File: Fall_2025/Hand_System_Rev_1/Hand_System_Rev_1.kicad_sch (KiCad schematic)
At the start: 0 parts

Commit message: Changes
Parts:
- added C1: 22u, Capacitor_THT:CP_Radial_D4.0mm_P1.50mm, symbol Device:C
- added C2: 100 μF, symbol Device:C
- added H1, H2, H3, H4: MountingHole, symbol Mechanical:MountingHole
- added J1: Barrel_Jack, Connector_BarrelJack:BarrelJack_SwitchcraftConxall_RAPC10U_Horizontal, symbol Connector:Barrel_Jack
- added M1, M2, M3, M4, M5, M6: Motor_Servo, Connector_PinHeader_2.54mm:PinHeader_1x03_P2.54mm_Vertical, symbol Motor:Motor_Servo
- added M7: Stepper_Motor, Connector_PinHeader_2.54mm:PinHeader_1x04_P2.54mm_Vertical, symbol Motor:Stepper_Motor_bipolar
- added U1: ESP32-DEVKITC-32UE, ESP32-DEVKITC-32UE:ESPRESSIF_ESP32-DEVKITC-32UE, symbol Schematic:ESP32-DEVKITC-32UE
- added U2: LM2596, symbol Schematic:LM2596
- added U3: A4988_Stepper_Motor_Driver, Module:Pololu_Breakout-16_15.2x20.3mm, symbol Driver_Motor:Pololu_Breakout_A4988
- added U4: ~, symbol Schematic:Rotary_Encoder
- added U5: MAX9814, MAX9814ETD_T:SON40P300X300X80-15N, symbol Schematic:MAX9814
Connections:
- net GND: now also C1.2, C2.2, J1.2, M1.3 (PWM), M2.3 (PWM), M3.3 (PWM), M4.3 (PWM), M5.3 (PWM), M6.3 (PWM), U1.14 (GND), U1.20 (GND__1), U1.26 (GND__2), U2.2 (GND), U2.3 (GND), U3.1 (GND), U3.7 (GND), U3.9 (~{ENABLE}), U4. (DT)
- new net: M7.1, U3.6 (2B)
- new net: M7.2 (-), U3.5 (2A)
- new net: M7.3, U3.4 (1A)
- new net: M7.4, U3.3 (1B)
- new net 12V: C1.1, C2.1, J1.1, U2.1 (Vin), U3.8 (VMOT)
- new net 3.3V: U1.1 (3V3), U1.2 (EN), U3.2 (VDD), U4. (DT)
- new net 5V: U1.19 (5V)
- new net 7.2V: M1.2 (+), M2.2 (+), M3.2 (+), M4.2 (+), M5.2 (+), M6.2 (+), U2.4 (Vout)
- new net DIR_PIN: U3.16 (DIR)
- new net INDEX: M3.1 (-)
- new net MIDDLE: M4.1 (-)
- new net PINKIE: M6.1 (-)
- new net RING: M5.1 (-)
- new net STEP_PIN: U3.15 (STEP)
- new net THUMB_1: M1.1 (-)
- new net THUMB_2: M2.1 (-)
- no-connect marks 0 -> 2
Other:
- note added: "ESP32_WROOM_32UE_DEVKITA"
- note added: "FINGER MOTORS"
- note added: "LM2596 BUCK CONVERTER"
- note added: "MOUNTING HOLES"
- note added: "ROTARY ENCODER"
- note added: "STEPPER MOTOR"
- note removed: "Global Labels"

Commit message: added microphone
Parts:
- removed U5: MAX9814, MAX9814ETD_T:SON40P300X300X80-15N, symbol Schematic:MAX9814
- added C3: 0.1uF, Capacitor_SMD:C_0805_2012Metric, symbol Device:C
- added C4: 0.47uF, Capacitor_SMD:C_0805_2012Metric, symbol Device:C
- added C5: 470nF, Capacitor_SMD:C_0805_2012Metric, symbol Device:C
- added C6: 2.2uF, Capacitor_SMD:C_0805_2012Metric, symbol Device:C
- added C7: 1uF, Capacitor_SMD:C_0805_2012Metric, symbol Device:C
- added MK1: Microphone, Sensor_Audio:POM-2244P-C3310-2-R, symbol Device:Microphone
- added R1: 150k, Resistor_SMD:R_0805_2012Metric, symbol Device:R
- added R2: 100k, Resistor_SMD:R_0805_2012Metric, symbol Device:R
- added U5: MAX9814ETD_T, MAX9814ETD_T:SON40P300X300X80-15N, symbol MAX9814ETD_T:MAX9814ETD_T
- C1: footprint Capacitor_THT:CP_Radial_D4.0mm_P1.50mm -> Capacitor_SMD:C_0805_2012Metric
- C2: footprint (none) -> Capacitor_SMD:C_0805_2012Metric
- H1, H2, H3, H4: footprint (none) -> MountingHole:MountingHole_4.3mm_M4
- U2: footprint (none) -> PCB_Components:LM2596
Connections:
- net 3.3V: now also U4.1 (VCC), C7.1, U5.10 (GAIN), U5.2 (~{SHDN}), U5.5 (VDD); no longer U4. (DT)
- net DIR_PIN: now also U1.31 (16)
- net GND: now also U4.2 (GND), C4.1, C5.1, C6.1, C7.2, MK1.1 (-), R2.2, U5.15 (EP), U5.7 (GND), U5.9 (A/R); no longer U4. (DT)
- net INDEX: now also U1.9 (25)
- net MIDDLE: now also U1.10 (26)
- net PINKIE: now also U1.7 (32)
- net RING: now also U1.11 (27)
- net STEP_PIN: now also U1.35 (15)
- net THUMB_1: now also U1.22
- net THUMB_2: now also U1.21 (23)
- net MP_OUT: now reaches U1.8 (33)
- net MP_OUT: now also U5.6 (MICOUT)
- new net: C5.2, U5.1 (CT)
- new net: C4.2, U5.12 (BIAS)
- new net: C3.1, MK1.2 (+), R1.1, U5.13 (MICBIAS)
- new net: R1.2, R2.1, U5.14 (TH)
- new net: C6.2, U5.3 (CG)
- new net: C3.2, U5.8 (MICIN)
- no-connect marks 2 -> 30
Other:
- note added: "MICROPHONE"

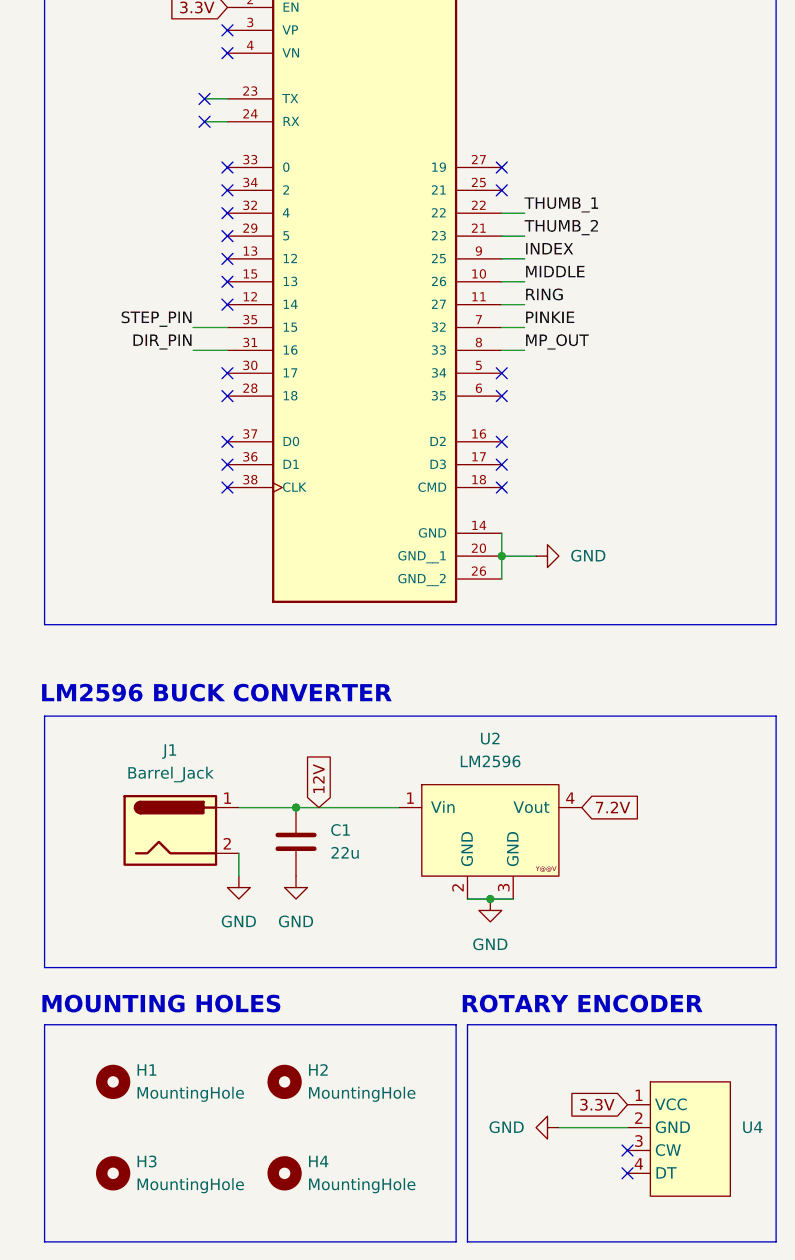
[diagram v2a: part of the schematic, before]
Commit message: creating kicad pcb schematic
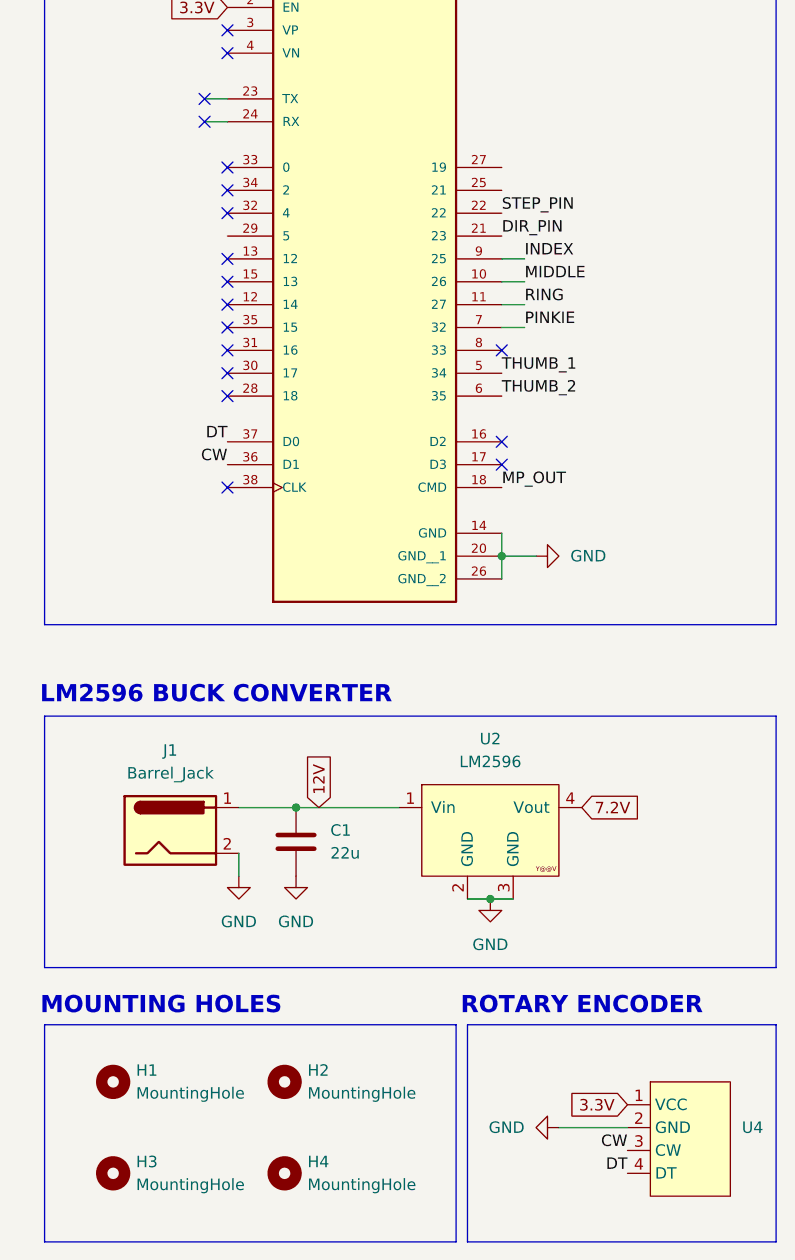
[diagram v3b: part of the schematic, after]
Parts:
- U1: footprint ESP32-DEVKITC-32UE:ESPRESSIF_ESP32-DEVKITC-32UE -> DEVKIT_V1_ESP32-WROOM-32:MODULE_DEVKIT_V1_ESP32-WROOM-32
- U4: footprint (none) -> Connector_PinHeader_2.54mm:PinHeader_1x04_P2.54mm_Vertical
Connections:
- net DIR_PIN: now also U1.21 (23); no longer U1.31 (16)
- net MP_OUT: now also U1.18 (CMD); no longer U1.8 (33)
- net STEP_PIN: now also U1.22; no longer U1.35 (15)
- net THUMB_1: now also U1.5 (34); no longer U1.22
- net THUMB_2: now also U1.6 (35); no longer U1.21 (23)
- net CW: now reaches U4.3 (CW)
- net CW: now also U1.36 (D1)
- net DT: now reaches U4.4 (DT)
- net DT: now also U1.37 (D0)
- no-connect marks 30 -> 23
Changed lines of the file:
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@@
 	)
 	(no_connect
-		(at 35.56 88.9)
-	)
-	(no_connect
 		(at 123.19 146.05)
 	)
@@
 	)
 	(no_connect
-		(at 66.04 81.28)
+		(at 35.56 73.66)
 	)
 	(no_connect
@@
 	)
 	(no_connect
-		(at 66.04 91.44)
-	)
-	(no_connect
-		(at 66.04 78.74)
-	)
-	(no_connect
-		(at 80.01 167.64)
-	)
-	(no_connect
 		(at 35.56 55.88)
 	)
@@
 	)
 	(no_connect
-		(at 80.01 165.1)
-	)
-	(no_connect
 		(at 123.19 140.97)
 	)
@@
 	)
 	(no_connect
-		(at 66.04 58.42)
-	)
-	(no_connect
-		(at 35.56 63.5)
-	)
-	(no_connect
 		(at 33.02 50.8)
 	)
 	(no_connect
-		(at 66.04 55.88)
+		(at 35.56 76.2)
 	)
 	(no_connect
-		(at 35.56 86.36)
+		(at 66.04 76.2)
 	)
 	(no_connect
@@
 	(wire
 		(pts
-			(xy 68.58 76.2) (xy 66.04 76.2)
-		)
-		(stroke
-			(width 0)
-			(type default)
-		)
-	)
-	(wire
-		(pts
 			(xy 146.05 133.35) (xy 147.32 133.35)
 		)
@@
 	(wire
 		(pts
-			(xy 68.58 60.96) (xy 66.04 60.96)
-		)
-		(stroke
-			(width 0)
-			(type default)
-		)
-	)
-	(wire
-		(pts
 			(xy 148.59 152.4) (xy 163.83 152.4)
 		)
@@
 	(wire
 		(pts
-			(xy 31.75 76.2) (xy 35.56 76.2)
-		)
-		(stroke
-			(width 0)
-			(type default)
-		)
-	)
-	(wire
-		(pts
 			(xy 111.76 130.81) (xy 123.19 130.81)
 		)
@@
 	(wire
 		(pts
-			(xy 68.58 63.5) (xy 66.04 63.5)
-		)
-		(stroke
-			(width 0)
-			(type default)
-		)
-	)
-	(wire
-		(pts
 			(xy 138.43 107.95) (xy 138.43 110.49)
 		)
@@
 	(wire
 		(pts
-			(xy 31.75 73.66) (xy 35.56 73.66)
-		)
-		(stroke
-			(width 0)
-			(type default)
-		)
-	)
-	(wire
-		(pts
 			(xy 195.58 77.47) (xy 181.61 77.47)
 		)
@@
 		)
 	)
+	(label "DT"
+		(at 80.01 167.64 180)
+		(effects
+			(font
+				(size 1.27 1.27)
+			)
+			(justify right bottom)
+		)
+	)
 	(label "RING"
 		(at 125.73 71.12 180)
@@
 	)
 	(label "STEP_PIN"
-		(at 31.75 73.66 180)
+		(at 66.04 60.96 0)
+		(effects
+			(font
+				(size 1.27 1.27)
+			)
+			(justify left bottom)
+		)
+	)
+	(label "DT"
+		(at 35.56 86.36 180)
 		(effects
 			(font
@@
 	)
 	(label "DIR_PIN"
-		(at 31.75 76.2 180)
+		(at 66.04 63.5 0)
+		(effects
+			(font
+				(size 1.27 1.27)
+			)
+			(justify left bottom)
+		)
+	)
+	(label "CW"
+		(at 80.01 165.1 180)
 		(effects
 			(font
@@
 	)
 	(label "MP_OUT"
-		(at 68.58 76.2 0)
+		(at 66.04 91.44 0)
 		(effects
 			(font
@@
 		)
 	)
+	(label "CW"
+		(at 35.56 88.9 180)
+		(effects
+			(font
+				(size 1.27 1.27)
+			)
+			(justify right bottom)
+		)
+	)
 	(label "THUMB_1"
-		(at 68.58 60.96 0)
+		(at 66.04 78.74 0)
 		(effects
 			(font
@@
 	)
 	(label "THUMB_2"
-		(at 68.58 63.5 0)
+		(at 66.04 81.28 0)
 		(effects
 			(font
@@
 			)
 		)
-		(property "Footprint" ""
+		(property "Footprint" "Connector_PinHeader_2.54mm:PinHeader_1x04_P2.54mm_Vertical"
 			(at 86.36 163.83 0)
 			(effects
@@
 			)
 		)
-		(property "Footprint" "ESP32-DEVKITC-32UE:ESPRESSIF_ESP32-DEVKITC-32UE"
+		(property "Footprint" "DEVKIT_V1_ESP32-WROOM-32:MODULE_DEVKIT_V1_ESP32-WROOM-32"
 			(at 50.8 63.5 0)
 			(effects

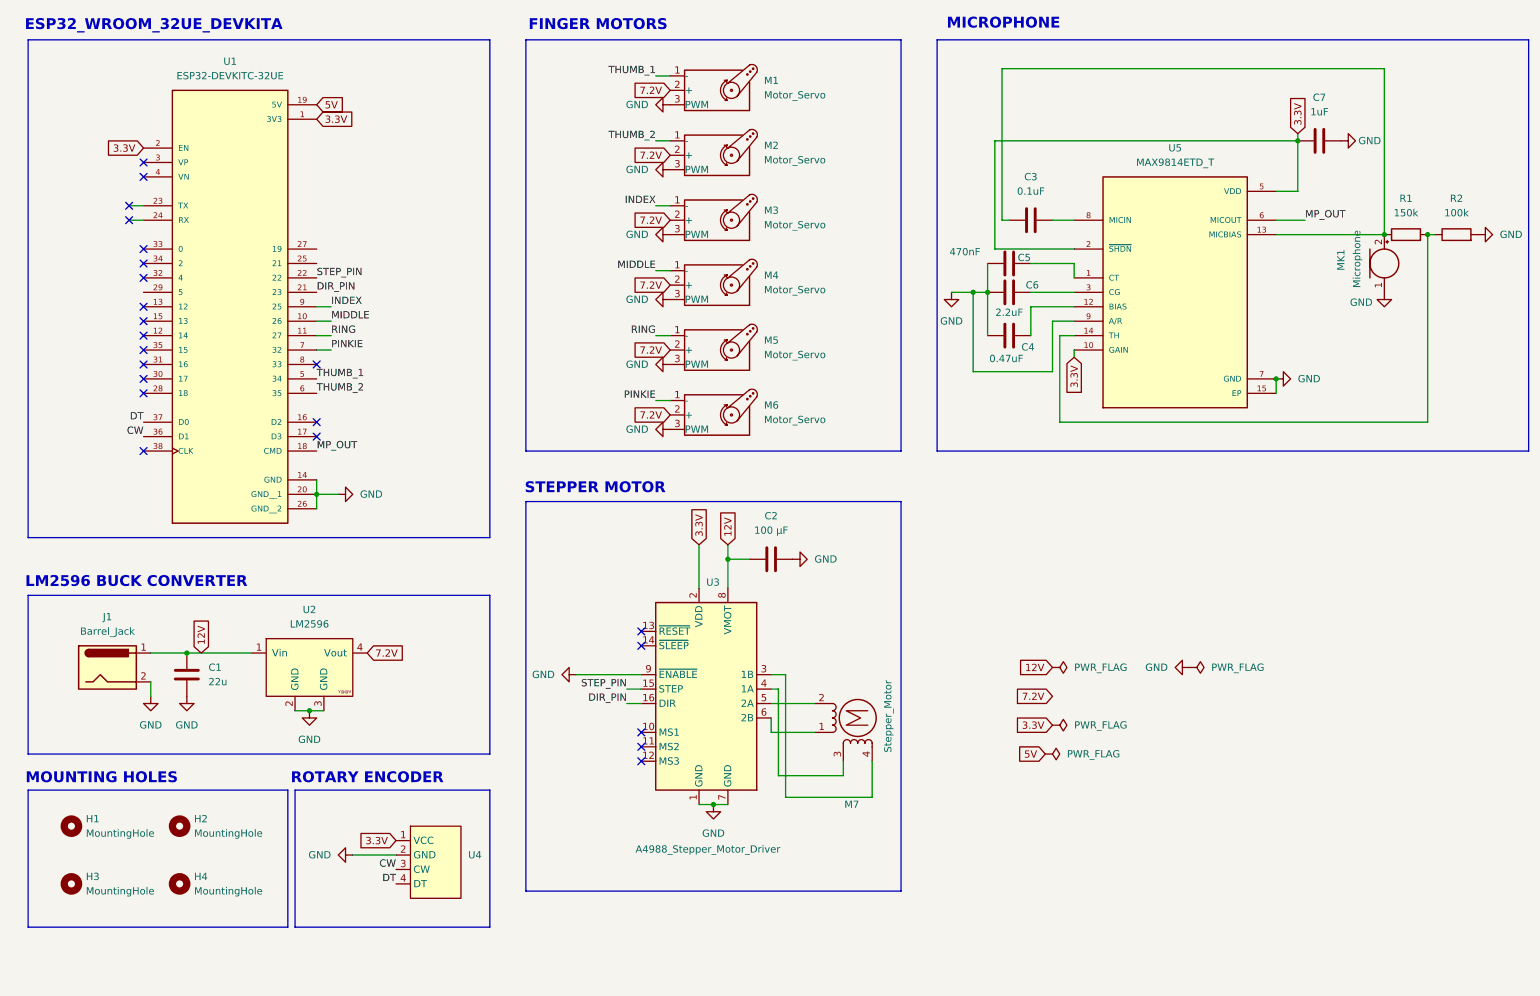
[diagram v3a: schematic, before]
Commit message: Finalized the pcb design
Included microphone and other modules.

Successfully got gerber files, drill files, and bom
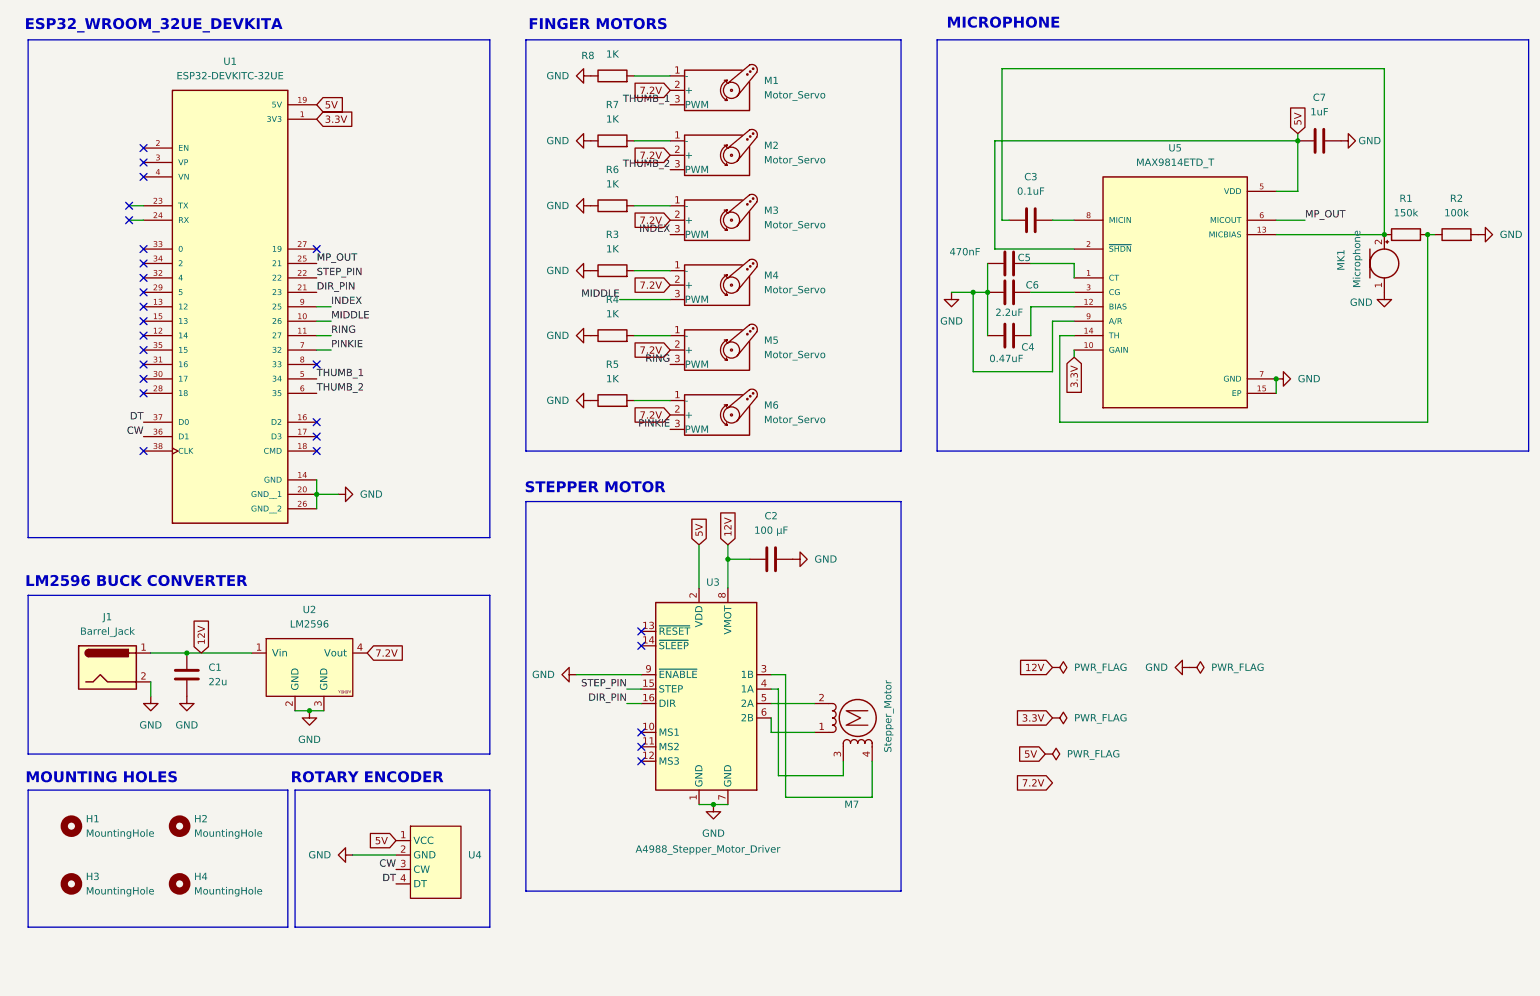
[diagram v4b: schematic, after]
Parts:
- added R3, R4, R5, R6, R7, R8: 1K, Resistor_SMD:R_0805_2012Metric, symbol Device:R
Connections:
- net 3.3V: no longer C7.1, U1.2 (EN), U3.2 (VDD), U4.1 (VCC), U5.2 (~{SHDN}), U5.5 (VDD)
- net 5V: now also C7.1, U3.2 (VDD), U4.1 (VCC), U5.2 (~{SHDN}), U5.5 (VDD)
- net GND: now also R3.1, R4.1, R5.1, R6.1, R7.1, R8.1; no longer M1.3 (PWM), M2.3 (PWM), M3.3 (PWM), M4.3 (PWM), M5.3 (PWM), M6.3 (PWM)
- net INDEX: now also M3.3 (PWM); no longer M3.1 (-)
- net MIDDLE: now also M4.3 (PWM); no longer M4.1 (-)
- net MP_OUT: now also U1.25 (21); no longer U1.18 (CMD)
- net PINKIE: now also M6.3 (PWM); no longer M6.1 (-)
- net RING: now also M5.3 (PWM); no longer M5.1 (-)
- net THUMB_1: now also M1.3 (PWM); no longer M1.1 (-)
- net THUMB_2: now also M2.3 (PWM); no longer M2.1 (-)
- new net: M2.1 (-), R7.2
- new net: M3.1 (-), R6.2
- new net: M6.1 (-), R5.2
- new net: M5.1 (-), R4.2
- new net: M4.1 (-), R3.2
- new net: M1.1 (-), R8.2
- no-connect marks 23 -> 27
